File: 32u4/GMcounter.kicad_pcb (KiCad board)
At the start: 2 copper layers, 120.4 x 29 mm, 44 parts, among them P1 CONN_01X01, P2 CONN_01X01, P3 CONN_01X01, P4 USB_A, P5 CONN_01X03, P6 CONN_02X04, P7 CONN_01X03, Q1 MMBT3904, Q2 STL128DN, Q3 MMBT3904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

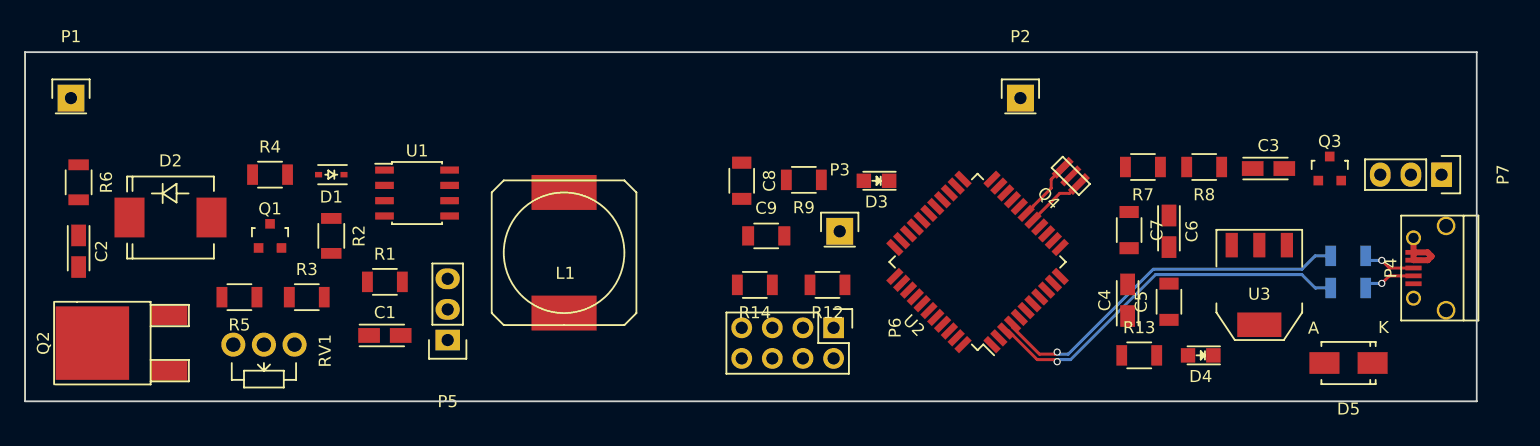
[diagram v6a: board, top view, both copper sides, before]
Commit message: updated to kicad 5
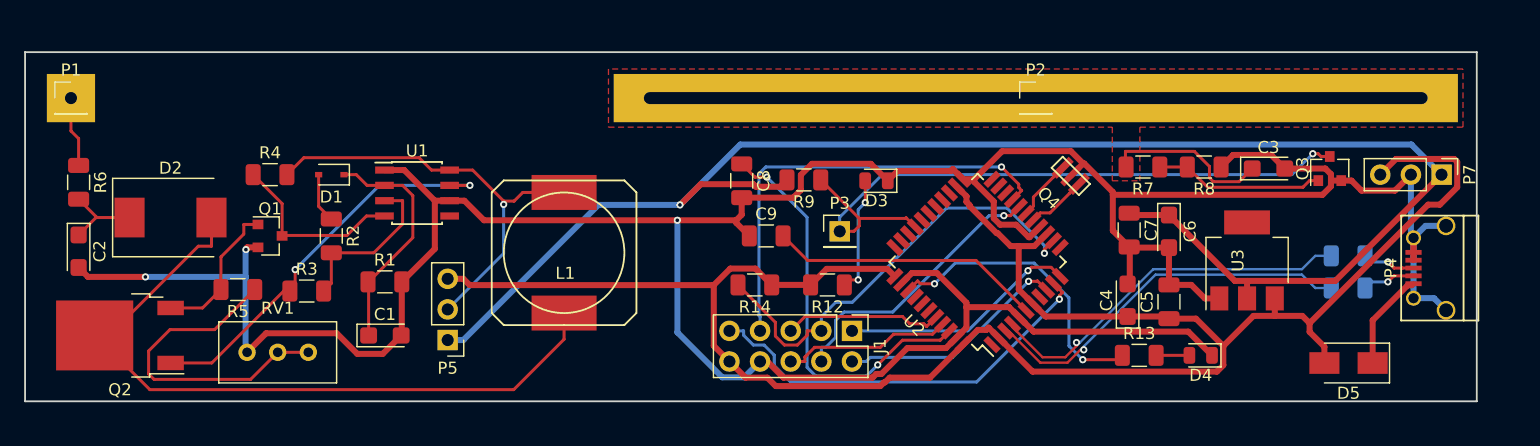
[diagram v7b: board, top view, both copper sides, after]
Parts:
- removed P6: CONN_02X04, Pin_Headers:Pin_Header_Straight_2x04
- added J1: Conn_02x05_Counter_Clockwise, Connector_PinHeader_2.54mm:PinHeader_2x05_P2.54mm_Vertical, F.Cu at (132.1, 76.5)
- C1, C2, C3, C4, C6: footprint Capacitors_Tantalum_SMD:TantalC_SizeA_EIA-3216_Reflow -> Capacitor_Tantalum_SMD:CP_EIA-3216-12_Kemet-S
- C5, C7, C8, C9: footprint Capacitors_SMD:C_1206 -> Capacitor_SMD:C_1206_3216Metric
- D1: footprint Diodes_SMD:SOD-323 -> Diode_SMD:D_SOD-323
- D2: footprint Diodes_SMD:SMC_Standard -> Diode_SMD:D_SMC
- D3, D4: footprint LEDs:LED_0805 -> Diode_SMD:D_0805_2012Metric
- D5: footprint Diodes_SMD:SMA_Standard -> Diode_SMD:D_SMA
- P1, P2, P3: footprint Pin_Headers:Pin_Header_Straight_1x01 -> Connector_PinHeader_2.54mm:PinHeader_1x01_P2.54mm_Vertical
- P5, P7: footprint Pin_Headers:Pin_Header_Straight_1x03 -> Connector_PinHeader_2.54mm:PinHeader_1x03_P2.54mm_Vertical
- Q1, Q3: footprint TO_SOT_Packages_SMD:SOT-23 -> Package_TO_SOT_SMD:SOT-23
- Q2: footprint TO_SOT_Packages_SMD:TO-252-2Lead -> Package_TO_SOT_SMD:TO-252-2
- R1, R10, R11, R12, R13, R14, R2, R3, R4, R5, R6, R7, R8, R9: footprint Resistors_SMD:R_1206 -> Resistor_SMD:R_1206_3216Metric
- RV1: footprint Potentiometers:Potentiometer_WirePads_Small -> Potentiometer_THT:Potentiometer_Bourns_3296W_Vertical
- U1: footprint Housings_SOIC:SOIC-8_3.9x4.9mm_Pitch1.27mm -> Package_SO:SOIC-8_3.9x4.9mm_P1.27mm
- U2: footprint Housings_QFP:TQFP-44_10x10mm_Pitch0.8mm -> Package_QFP:TQFP-44_10x10mm_P0.8mm
- U3: footprint TO_SOT_Packages_SMD:SOT-223 -> Package_TO_SOT_SMD:SOT-223
- moved Q2 4.11 mm to (71.4, 76.8), turned to 180 degrees
- moved U3 2.27 mm to (164.8, 70.6), turned to 90 degrees
- moved RV1 1.31 mm to (87.0, 78.2), turned to 0 degrees
- moved P2 1.27 mm to (147.3, 57.1)
- moved R5 0.65 mm to (81.2, 73.0)
- moved R3 0.51 mm to (86.9, 73.2)
- turned Q3 to 90 degrees
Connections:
- U1 pad 5: (no net) -> Net-(U1-Pad5)
- U2 pad 1: (no net) -> Net-(U2-Pad1)
- U2 pad 12: (no net) -> Net-(U2-Pad12)
- U2 pad 20: (no net) -> Net-(U2-Pad20)
- U2 pad 21: (no net) -> Net-(U2-Pad21)
- U2 pad 22: (no net) -> Net-(U2-Pad22)
- U2 pad 25: (no net) -> Net-(U2-Pad25)
- U2 pad 26: (no net) -> Net-(U2-Pad26)
- U2 pad 27: (no net) -> Net-(U2-Pad27)
- U2 pad 28: (no net) -> Net-(U2-Pad28)
- U2 pad 29: (no net) -> Net-(U2-Pad29)
- U2 pad 31: (no net) -> Net-(U2-Pad31)
- U2 pad 32: (no net) -> Net-(U2-Pad32)
- U2 pad 33: (no net) -> Net-(U2-Pad33)
- U2 pad 37: (no net) -> Net-(U2-Pad37)
- U2 pad 38: (no net) -> Net-(U2-Pad38)
- U2 pad 39: (no net) -> Net-(U2-Pad39)
- U2 pad 40: (no net) -> ADC1
- U2 pad 41: (no net) -> ADC0
- U2 pad 8: (no net) -> Net-(U2-Pad8)
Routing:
- net GND: track 5.55 -> 275.5 mm, vias 0 -> 3
- net +5V: track 0.00 -> 165.8 mm
- net +3V3: track 0.00 -> 133.4 mm, vias 0 -> 1
- net Net-(D2-Pad2): track 0.00 -> 59.5 mm
- net PULSE: track 0.00 -> 56.0 mm, vias 0 -> 1
- net SDA: track 0.00 -> 37.1 mm, vias 0 -> 1
- net RST: track 0.00 -> 37.1 mm, vias 0 -> 1
- net Net-(L1-Pad2): track 0.00 -> 36.3 mm, vias 0 -> 1
- net MOSI: track 0.00 -> 34.4 mm, vias 0 -> 1
- net Net-(Q2-Pad1): track 0.00 -> 33.4 mm, vias 0 -> 2
- net Net-(C8-Pad1): track 0.00 -> 33.3 mm, vias 0 -> 2
- net Net-(R5-Pad1): track 0.00 -> 27.2 mm
- net Net-(R13-Pad1): track 0.00 -> 24.7 mm, vias 0 -> 2
- net SCL: track 0.00 -> 23.3 mm, vias 0 -> 1
- net Net-(C9-Pad2): track 0.00 -> 22.7 mm
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- added copper zone on F.Cu, net Net-(C3-Pad1)

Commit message: first version to printer
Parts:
- added REF**: SRR1208, SRR1208, F.Cu at (0.00, 0.00)
- L1: footprint Inductors:SELF-WE-PD-XXL -> MyKiCadLibs:SRR1208
- moved L1 2.47 mm to (107.7, 72.4), turned to 270 degrees
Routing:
- net +5V: track 165.8 -> 136.4 mm
- net Net-(R5-Pad1): track 27.2 -> 8.54 mm, vias 0 -> 1
- net Net-(Q2-Pad1): track 33.4 -> 45.4 mm, vias 2 -> 0
- net SDA: track 37.1 -> 27.9 mm
- net SCL: track 23.3 -> 31.1 mm, vias 1 -> 0
- net Net-(C8-Pad1): track 33.3 -> 25.6 mm
- net +3V3: track 133.4 -> 128.3 mm
- net Net-(D2-Pad2): track 59.5 -> 55.1 mm
- net PULSE: track 56.0 -> 59.4 mm
- net Net-(L1-Pad2): track 36.3 -> 39.2 mm
- net MISO: track 19.8 -> 21.9 mm
- net RST: track 37.1 -> 34.9 mm
- net Net-(Q3-Pad1): track 14.1 -> 15.5 mm
- net SCLK: track 19.2 -> 20.4 mm
- net MOSI: track 34.4 -> 33.4 mm
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- added copper zone on B.Cu, net GND
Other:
- net class Default: clearance 0.2 -> 0.25
- net class highA: clearance 0.2 -> 0.25; trace_width 0.5 -> 0.3
- rule pad_to_mask_clearance: 0.2 -> 0.3
- rule trace_clearance: 0.2 -> 0.25
- board text added: "GMCounter 32u4 Takigama@github"
